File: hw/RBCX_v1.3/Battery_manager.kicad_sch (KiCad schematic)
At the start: 78 parts

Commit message: Work in progress
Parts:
- removed Q? (x2): Q_PMOS_DGS, Package_TO_SOT_SMD:SOT-723, symbol Device:Q_PMOS_DGS
- removed Q? (x4): 2N7002KDW, Package_TO_SOT_SMD:SOT-363_SC-70-6, symbol RBCX:2N7002KDW
- removed Q?: Q_PMOS_DGS, RBCX:U-DFN2020-6-EP, symbol Device:Q_PMOS_DGS
- removed R? (x2): 10k, Capacitor_SMD:C_0201_0603Metric, symbol Device:R
- removed R? (x2): 33R, Capacitor_SMD:C_0805_2012Metric, symbol Device:R
- removed U? (x2): HY2213-BB3A, Package_TO_SOT_SMD:SOT-23-6, symbol RBCX:HY2213-BB3A
- added C? (x2): 100nF, Capacitor_SMD:C_0402_1005Metric, symbol Device:C
- added Q11: JSM3622, RBCX:JSM3622, symbol RBCX:JSM3622
- added Q? (x2): 2N7002KDW, Package_TO_SOT_SMD:SOT-363_SC-70-6, symbol RBCX:2N7002KDW
- added Q? (x3): Q_PMOS_DGS, Package_TO_SOT_SMD:SOT-723, symbol Device:Q_PMOS_DGS
- added Q? (x2): Q_NMOS_DGS, Package_TO_SOT_SMD:SOT-723, symbol Device:Q_NMOS_DGS
- added R? (x2): 33R, Capacitor_SMD:C_0805_2012Metric, symbol Device:R
- added R? (x2): 100, Capacitor_SMD:C_0402_1005Metric, symbol Device:R
- added R? (x2): 10k, Capacitor_SMD:C_0201_0603Metric, symbol Device:R
- added U? (x2): HY2213-BB3A, Package_TO_SOT_SMD:SOT-23-6, symbol RBCX:HY2213-BB3A
- D24: renamed from D?; footprint Package_TO_SOT_SMD:SOT-23 -> Package_TO_SOT_SMD:SOT-523; LCSC C2828465 -> C134414
- SW13, SW14: renamed from SW?; footprint Button_Switch_SMD:SW_Push_1P1T_NO_CK_KSC6xxJ -> RBCX:SW
- gave numbers to parts that had none: 56
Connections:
- net BAT+: now also Q12.3 (D); no longer Q12.1 (S)
- net BAT+_PROTECTED: now also Q12.1 (S), Q12.4 (S); no longer Q12.3 (D), Q13.6 (D)
- net BAT_MID: now also Q?.1 (D), R?.1; no longer R155.1
- net BUTTON_ON_ORIGINAL: now also Q?.2 (G)
- net CHARGER_INPUT: now also Q10.6 (D); no longer Q10.4 (S)
- net GND: now also C?.1, Q?.1 (S), Q?.3 (S), Q?.3 (S), R?.1, U?.3 (VSS)
- net PWRSW: now also Q?.1 (D)
- net VCC: now also Q13.1 (S), Q13.4 (S), Q11.3 (D); no longer Q12.4 (S), Q13.3 (D)
- net VUSB: now also Q11.6 (D)
- net at C76.1, R169.1, R170.1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: now also Q?.2 (G)
- net at R168.2: now also Q?.1 (D)
- net at Q14.2 (G), Q15.2 (G), R167.1: now also Q10.3 (D), Q12.6 (D), Q13.3 (D), Q13.6 (D); no longer Q10.1 (S), Q13.1 (S), Q13.4 (S)
- net at R158.2, R161.2: now also Q11.2 (G), Q11.5 (G); no longer Q12.5 (G)
- net at R158.1: now also Q11.1 (S), Q11.4 (S); no longer Q12.6 (D)
- net at Q13.2 (G), Q15.6 (D), R159.2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: now also Q13.5 (G)
- net PWRON: now reaches R163.2, R166.2, TP55.P$1 (TP)
- net PWRON: now also Q12.5 (G), Q?.2 (G); no longer Q13.5 (G)
- new net: Q10.1 (S), Q10.4 (S), R157.2
- new net: Q?.3 (D), R?.2
- new net: Q?.5 (G), U?.6 (OUT)
- new net: Q?.6 (D), R?.2
- new net: Q?.2 (G), R?.2 (x2)
- new net: Q?.3 (S), R?.1, R?.2
- new net: C?.2, R?.1, U?.2 (VCC) (x2)
- new net: Q?.3 (S), Q?.3 (S)
- new net: Q?.2 (G), U?.6 (OUT)
- new net BAT+_ON: Q?.1 (D)
- new net BAT_MID_PROTECTED: C?.1, Q?.1 (D), Q?.4 (S), R155.1, R?.1, R?.2, U?.3 (VSS)
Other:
- note added: "Protection of Q12A gate over voltage spikes on power rail - makes filter together with gate capacitance"
- note added: "Protection of Q12B gate over voltage spikes on power rail makes filter together with gate capacitance"
- note removed: "Protection of Q1A gate over voltage spikes on power rail - makes filter together with gate capacitance"
- note removed: "Protection of Q1B gate over voltage spikes on power rail makes filter together with gate capacitance"
- moved on the sheet: C59, C60, C61, C62, C63, C64, C65, C66, C67, C68, C69, C70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

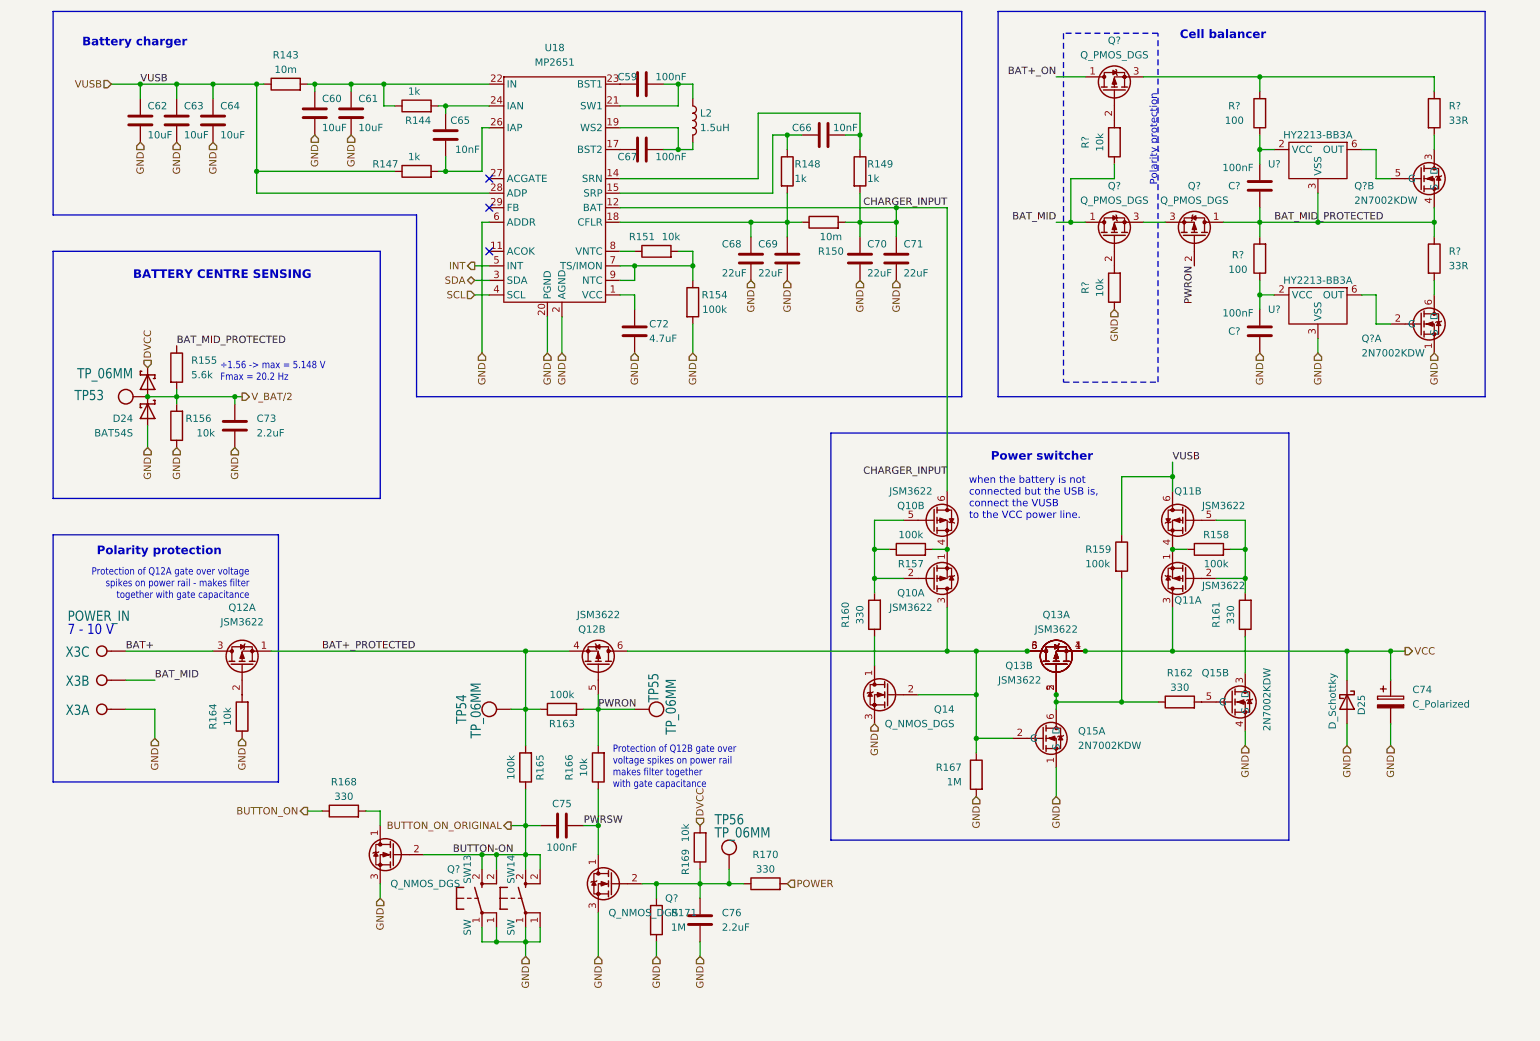
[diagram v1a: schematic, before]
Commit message: New PCB layout
some changes of schema:
- change PD sink AO33772 to AO33771
- remove power switch
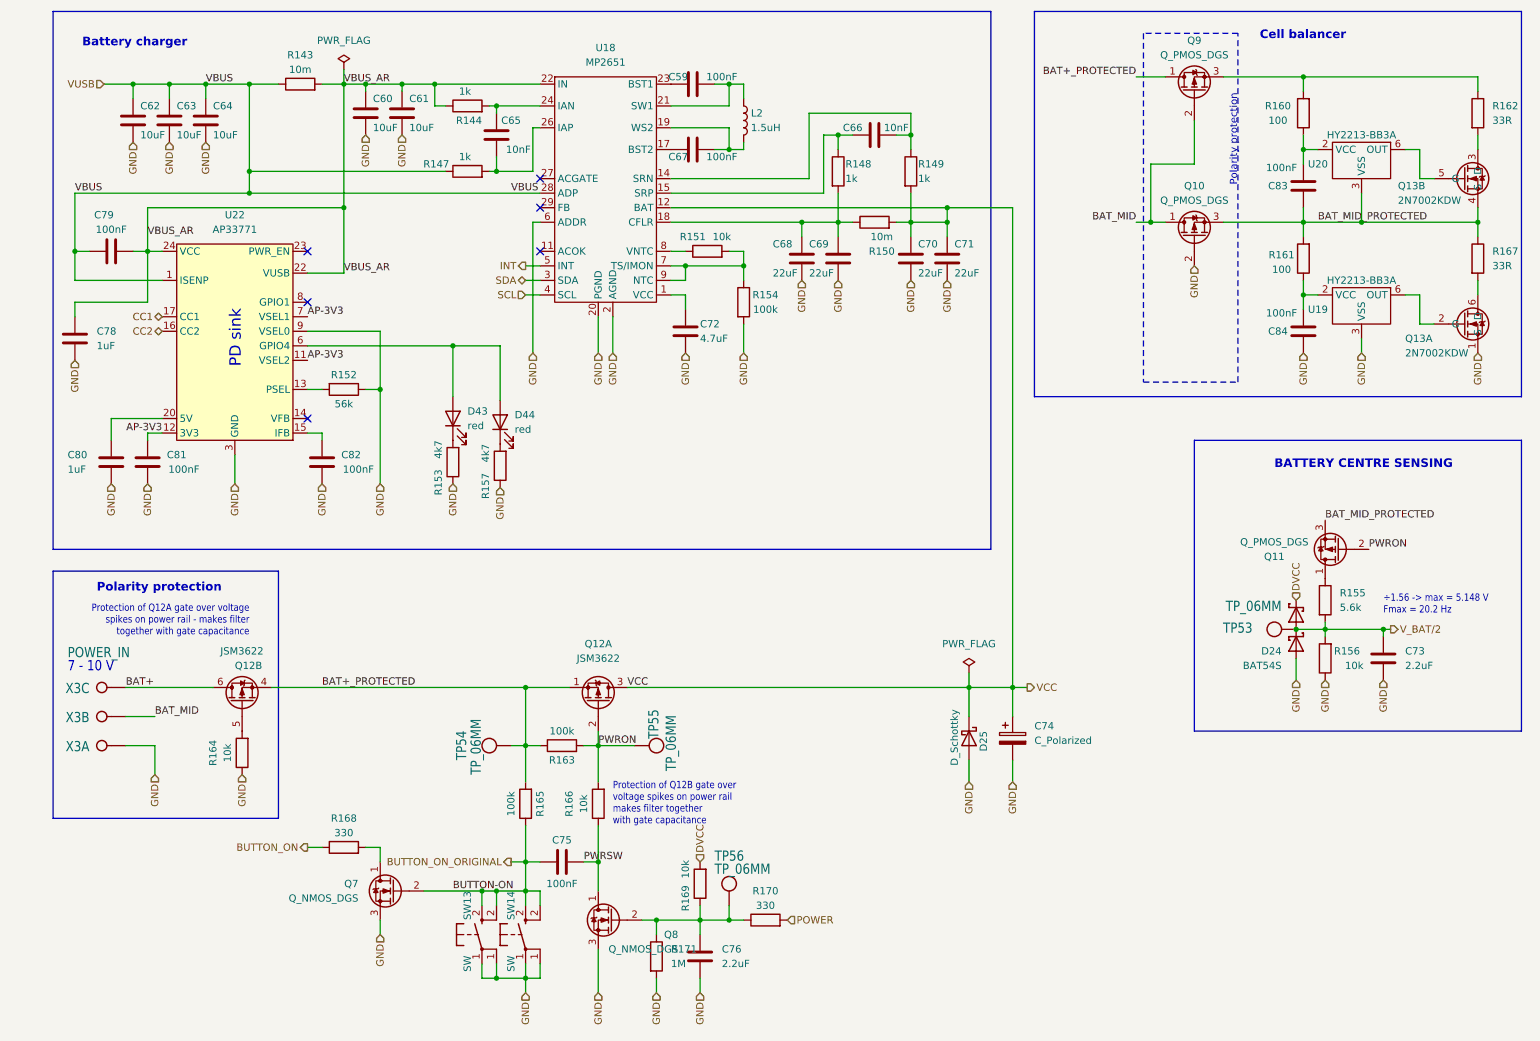
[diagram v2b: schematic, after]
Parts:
- removed Q10, Q11, Q13: JSM3622, RBCX:JSM3622, symbol RBCX:JSM3622
- removed Q14: Q_NMOS_DGS, Package_TO_SOT_SMD:SOT-723, symbol Device:Q_NMOS_DGS
- removed Q15: 2N7002KDW, Package_TO_SOT_SMD:SOT-363_SC-70-6, symbol RBCX:2N7002KDW
- removed R158, R159: 100k, Capacitor_SMD:C_0201_0603Metric, symbol Device:R
- removed R160, R161, R162: 330, Capacitor_SMD:C_0201_0603Metric, symbol Device:R
- removed R167: 1M, Resistor_SMD:R_0201_0603Metric, symbol Device:R
- removed R? (x2): 10k, Capacitor_SMD:C_0201_0603Metric, symbol Device:R
- added C78, C80: 1uF, Resistor_SMD:R_0402_1005Metric, symbol Device:C
- added C79, C81, C82: 100nF, Capacitor_SMD:C_0402_1005Metric, symbol Device:C
- added D43, D44: red, LED_SMD:LED_0603_1608Metric, symbol Device:LED
- added R152: 56k, Capacitor_SMD:C_0402_1005Metric, symbol Device:R
- added R153: 4k7, Resistor_SMD:R_0201_0603Metric, symbol Device:R
- added U22: AP33771, Package_DFN_QFN:QFN-24-1EP_4x4mm_P0.5mm_EP2.6x2.6mm, symbol RBCX:AP33771
- R157: value 100k -> 4k7; footprint Capacitor_SMD:C_0201_0603Metric -> Resistor_SMD:R_0201_0603Metric; LCSC C270364 -> C270346
- gave numbers to parts that had none: 14
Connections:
- net BAT+_ON is gone; now on net BAT+_PROTECTED: Q9.1 (D)
- net CHARGER_INPUT is gone; now on net VCC: C70.1, C71.1, R149.2, R150.2, U18.12 (BAT)
- net BAT+: now also Q12.6 (D); no longer Q12.3 (D)
- net BAT_MID: now also Q9.2 (G)
- net BAT_MID_PROTECTED: now also Q10.3 (S), Q11.3 (S); no longer Q11.1 (D), R155.1
- net GND: now also Q10.2 (G), R157.1, C78.2, C80.2, C81.1, C82.1, R152.1, R153.1, U22.25 (GND), U22.3 (GND), U22.9 (VSEL0)
- net PWRON: now also Q12.2 (G); no longer Q12.5 (G)
- net VCC: now also Q12.3 (D)
- net VUSB: now also C79.1, U22.1 (ISENP)
- net at R164.2: now also Q12.5 (G); no longer Q12.2 (G)
- net VBUS_AR: now reaches C60.1, C61.1, R143.2, R144.1, U18.22 (IN)
- net VBUS_AR: now also C78.1, C79.2, U22.22 (VUSB), U22.24 (VCC)
- net at R157.2: now also D44.1 (K)
- new net: Q11.1 (D), R155.1
- new net: D43.1 (K), R153.2
- new net: C80.1, U22.20 (5V)
- new net: C82.2, U22.15 (IFB)
- new net: R152.2, U22.13 (PSEL)
- new net: D43.2 (A), D44.2 (A), U22.6 (GPIO4)
- new net AP-3V3: C81.2, U22.11 (VSEL2), U22.12 (3V3), U22.7 (VSEL1)
- new net CC1: U22.17 (CC1)
- new net CC2: U22.16 (CC2)
- no-connect marks 3 -> 6
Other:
- note added: "PD sink"
- note removed: "Power switcher"
- note removed: "when the battery is not connected but the USB is, connect the VUSB to the VCC power line."
- moved on the sheet: C59, C60, C61, C62, C63, C64, C65, C66, C67, C68, C69, C70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

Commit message: Production files
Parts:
- D24, Q10, Q11, Q7, Q8, Q9, U19, U20: JLCPCB_CORRECTION (none) -> 0;0;180
- Q13: JLCPCB_CORRECTION (none) -> 0;0;-90
- TP53, TP54, TP55, TP56, X3: JLCPCB_IGNORE (none) -> 1
- U18: JLCPCB (none) -> 1589-MP2651GVT-0000-ZCT-ND
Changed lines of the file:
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@@
+      (effects (font (size 1.27 1.27)) hide)
+    )
+    (property "JLCPCB_IGNORE" "1" (id 4) (at 30.48 146.05 0)
       (effects (font (size 1.27 1.27)) hide)
     )
@@
       (effects (font (size 1.27 1.27)) hide)
     )
+    (property "JLCPCB_IGNORE" "1" (id 4) (at 240.03 125.73 0)
+      (effects (font (size 1.27 1.27)) hide)
+    )
     (pin "P$1")
   )
@@
     )
     (property "Datasheet" "https://www.monolithicpower.com/en/documentview/productdocument/index/version/2/document_type/Datasheet/lang/en/sku/MP2651GVT/document_id/9948/" (id 3) (at 119.38 30.48 0)
+      (effects (font (size 1.27 1.27)) hide)
+    )
+    (property "JLCPCB" "1589-MP2651GVT-0000-ZCT-ND" (id 4) (at 119.38 30.48 0)
       (effects (font (size 1.27 1.27)) hide)
     )
@@
       (effects (font (size 1.27 1.27)) hide)
     )
+    (property "JLCPCB_CORRECTION" "0;0;-90" (id 6) (at 271.78 46.99 0)
+      (effects (font (size 1.27 1.27)) hide)
+    )
     (pin "1")
     (pin "2")
@@
       (effects (font (size 1.27 1.27)) hide)
     )
+    (property "JLCPCB_CORRECTION" "0;0;180" (id 6) (at 222.25 31.75 0)
+      (effects (font (size 1.27 1.27)) hide)
+    )
     (pin "1")
     (pin "2")
@@
       (effects (font (size 1.27 1.27)) hide)
     )
+    (property "JLCPCB_IGNORE" "1" (id 4) (at 140.97 173.99 0)
+      (effects (font (size 1.27 1.27)) hide)
+    )
     (pin "P$1")
   )
@@
     )
     (property "Datasheet" "" (id 3) (at 30.48 135.89 0)
+      (effects (font (size 1.27 1.27)) hide)
+    )
+    (property "JLCPCB_IGNORE" "1" (id 4) (at 30.48 135.89 0)
       (effects (font (size 1.27 1.27)) hide)
     )
@@
       (effects (font (size 1.27 1.27)) hide)
     )
+    (property "JLCPCB_CORRECTION" "0;0;180" (id 6) (at 247.65 111.76 0)
+      (effects (font (size 1.27 1.27)) hide)
+    )
     (pin "1")
     (pin "2")
@@
       (effects (font (size 1.27 1.27)) hide)
     )
+    (property "JLCPCB_IGNORE" "1" (id 4) (at 30.48 140.97 0)
+      (effects (font (size 1.27 1.27)) hide)
+    )
     (pin "1")
     (pin "2")
@@
       (effects (font (size 1.27 1.27)) hide)
     )
+    (property "JLCPCB_CORRECTION" "0;0;180" (id 6) (at 120.65 176.53 0)
+      (effects (font (size 1.27 1.27)) hide)
+    )
     (pin "1")
     (pin "2")
@@
       (effects (font (size 1.27 1.27)) hide)
     )
+    (property "JLCPCB_CORRECTION" "0;0;180" (id 6) (at 251.46 41.91 0)
+      (effects (font (size 1.27 1.27)) hide)
+    )
     (pin "2")
     (pin "3")
@@
       (effects (font (size 1.27 1.27)) hide)
     )
+    (property "JLCPCB_CORRECTION" "0;0;180" (id 6) (at 222.25 57.15 0)
+      (effects (font (size 1.27 1.27)) hide)
+    )
     (pin "1")
     (pin "2")
@@
     )
     (property "Basic/Extended" "E" (id 5) (at 251.46 67.31 0)
+      (effects (font (size 1.27 1.27)) hide)
+    )
+    (property "JLCPCB_CORRECTION" "0;0;180" (id 6) (at 251.46 67.31 0)
       (effects (font (size 1.27 1.27)) hide)
     )
@@
       (effects (font (size 1.27 1.27)) hide)
     )
+    (property "JLCPCB_CORRECTION" "0;0;-90" (id 6) (at 271.78 72.39 0)
+      (effects (font (size 1.27 1.27)) hide)
+    )
     (pin "1")
     (pin "2")
@@
       (effects (font (size 1.27 1.27)) hide)
     )
+    (property "JLCPCB_CORRECTION" "0;0;180" (id 6) (at 240.03 125.73 0)
+      (effects (font (size 1.27 1.27)) hide)
+    )
     (pin "1")
     (pin "2")
@@
       (effects (font (size 1.27 1.27)) hide)
     )
+    (property "JLCPCB_IGNORE" "1" (id 4) (at 102.87 146.05 0)
+      (effects (font (size 1.27 1.27)) hide)
+    )
     (pin "P$1")
   )
@@
       (effects (font (size 1.27 1.27)) hide)
     )
+    (property "JLCPCB_CORRECTION" "0;0;180" (id 6) (at 82.55 171.45 0)
+      (effects (font (size 1.27 1.27)) hide)
+    )
     (pin "1")
     (pin "2")
@@
       (effects (font (size 1.27 1.27)) hide)
     )
+    (property "JLCPCB_IGNORE" "1" (id 4) (at 124.46 146.05 0)
+      (effects (font (size 1.27 1.27)) hide)
+    )

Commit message: Protective resistors for I2C on connectors
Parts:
- added R158: 10k, Capacitor_SMD:C_0201_0603Metric, symbol Device:R
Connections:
- net DVCC: now also R158.2
- net INT: now also R158.1
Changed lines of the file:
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@@
   (junction (at 128.27 176.53) (diameter 0) (color 0 0 0 0)
+  )
+  (junction (at 104.14 62.23) (diameter 0) (color 0 0 0 0)
   )
   (junction (at 43.18 30.48) (diameter 0) (color 0 0 0 0)
@@
     (stroke (width 0) (type default) (color 0 0 0 0))
   )
-  (wire (pts (xy 105.41 62.23) (xy 107.95 62.23))
+  (wire (pts (xy 101.6 62.23) (xy 104.14 62.23))
     (stroke (width 0) (type default) (color 0 0 0 0))
   )
@@
     (stroke (width 0) (type default) (color 0 0 0 0))
   )
+  (wire (pts (xy 104.14 62.23) (xy 104.14 58.42))
+    (stroke (width 0) (type default) (color 0 0 0 0))
+  )
   (wire (pts (xy 245.11 125.73) (xy 245.11 124.46))
     (stroke (width 0) (type default) (color 0 0 0 0))
@@
     (stroke (width 0) (type default) (color 0 0 0 0))
   )
-  (wire (pts (xy 105.41 64.77) (xy 107.95 64.77))
+  (wire (pts (xy 101.6 64.77) (xy 107.95 64.77))
     (stroke (width 0) (type default) (color 0 0 0 0))
   )
@@
     (stroke (width 0) (type default) (color 0 0 0 0))
   )
-  (wire (pts (xy 105.41 67.31) (xy 107.95 67.31))
+  (wire (pts (xy 101.6 67.31) (xy 107.95 67.31))
     (stroke (width 0) (type default) (color 0 0 0 0))
   )
@@
     (stroke (width 0) (type default) (color 0 0 0 0))
   )
+  (wire (pts (xy 104.14 58.42) (xy 101.6 58.42))
+    (stroke (width 0) (type default) (color 0 0 0 0))
+  )
   (wire (pts (xy 87.63 171.45) (xy 97.79 171.45))
     (stroke (width 0) (type default) (color 0 0 0 0))
@@
   )
   (wire (pts (xy 26.67 59.69) (xy 29.21 59.69))
+    (stroke (width 0) (type default) (color 0 0 0 0))
+  )
+  (wire (pts (xy 104.14 62.23) (xy 107.95 62.23))
     (stroke (width 0) (type default) (color 0 0 0 0))
   )
@@
     (effects (font (size 1.27 1.27)) (justify right))
   )
-  (hierarchical_label "INT" (shape output) (at 105.41 62.23 180)
+  (hierarchical_label "INT" (shape output) (at 101.6 62.23 180)
+    (effects (font (size 1.27 1.27)) (justify right))
+  )
+  (hierarchical_label "DVCC" (shape input) (at 93.98 58.42 180)
     (effects (font (size 1.27 1.27)) (justify right))
   )
@@
     (effects (font (size 1.27 1.27)) (justify right))
   )
-  (hierarchical_label "SDA" (shape bidirectional) (at 105.41 64.77 180)
+  (hierarchical_label "SDA" (shape bidirectional) (at 101.6 64.77 180)
     (effects (font (size 1.27 1.27)) (justify right))
   )
@@
     (effects (font (size 1.27 1.27)) (justify right))
   )
-  (hierarchical_label "SCL" (shape input) (at 105.41 67.31 180)
+  (hierarchical_label "SCL" (shape input) (at 101.6 67.31 180)
     (effects (font (size 1.27 1.27)) (justify right))
   )
@@
       (effects (font (size 1.27 1.27)) hide)
     )
+    (pin "1")
+    (pin "2")
+  )
+  (symbol (lib_id "Device:R") (at 97.79 58.42 270) (unit 1)
+    (in_bom yes) (on_board yes)
+    (property "Reference" "R158" (id 0) (at 93.98 55.88 90))
+    (property "Value" "10k" (id 1) (at 100.33 55.88 90))
+    (property "Footprint" "Capacitor_SMD:C_0201_0603Metric" (id 2) (at 97.79 56.642 90)
+      (effects (font (size 1.27 1.27)) hide)
+    )
+    (property "Datasheet" "~" (id 3) (at 97.79 58.42 0)
+      (effects (font (size 1.27 1.27)) hide)
+    )
+    (property "LCSC" "C106225" (id 4) (at 97.79 58.42 0)
+      (effects (font (size 1.27 1.27)) hide)
+    )
+    (property "Basic/Extended" "E" (id 5) (at 97.79 58.42 0)
+      (effects (font (size 1.27 1.27)) hide)
+    )
